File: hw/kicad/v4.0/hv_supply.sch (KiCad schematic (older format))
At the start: 32 parts, among them U4 ACT4088, U5 LNK304D

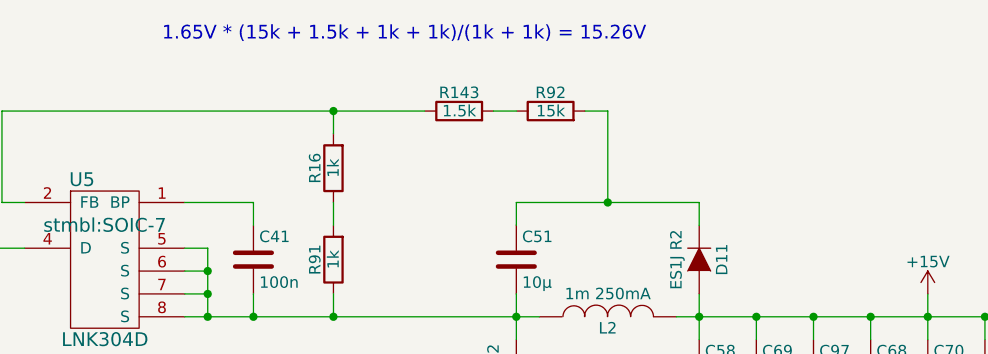
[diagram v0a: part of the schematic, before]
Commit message: changes for IKCM30F60GD
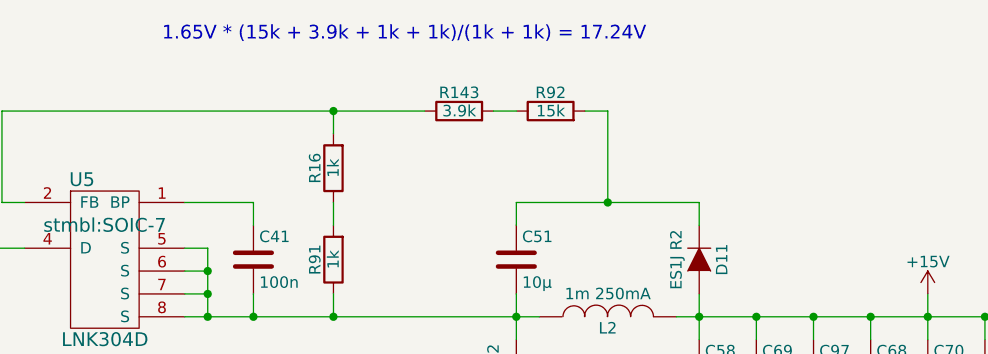
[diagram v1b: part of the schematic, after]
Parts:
- R143: value 1.5k -> 3.9k
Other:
- note added: "1.65V * (15k + 3.9k + 1k + 1k)/(1k + 1k) = 17.24V"
- note removed: "1.65V * (15k + 1.5k + 1k + 1k)/(1k + 1k) = 15.26V"
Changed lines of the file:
@@
 P 6150 3100
 F 0 "R143" V 6230 3100 50  0000 C CNN
-F 1 "1.5k" V 6150 3100 50  0000 C CNN
+F 1 "3.9k" V 6150 3100 50  0000 C CNN
 F 2 "stmbl:R_0603" V 6080 3100 30  0001 C CNN
 F 3 "" H 6150 3100 30  0000 C CNN
@@
 Connection ~ 6800 3500
 Text Notes 4850 2800 0    60   ~ 0
-1.65V * (15k + 1.5k + 1k + 1k)/(1k + 1k) = 15.26V
+1.65V * (15k + 3.9k + 1k + 1k)/(1k + 1k) = 17.24V
 Wire Wire Line
 	2850 6200 3250 6200
